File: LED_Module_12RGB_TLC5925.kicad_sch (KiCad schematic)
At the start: 0 parts

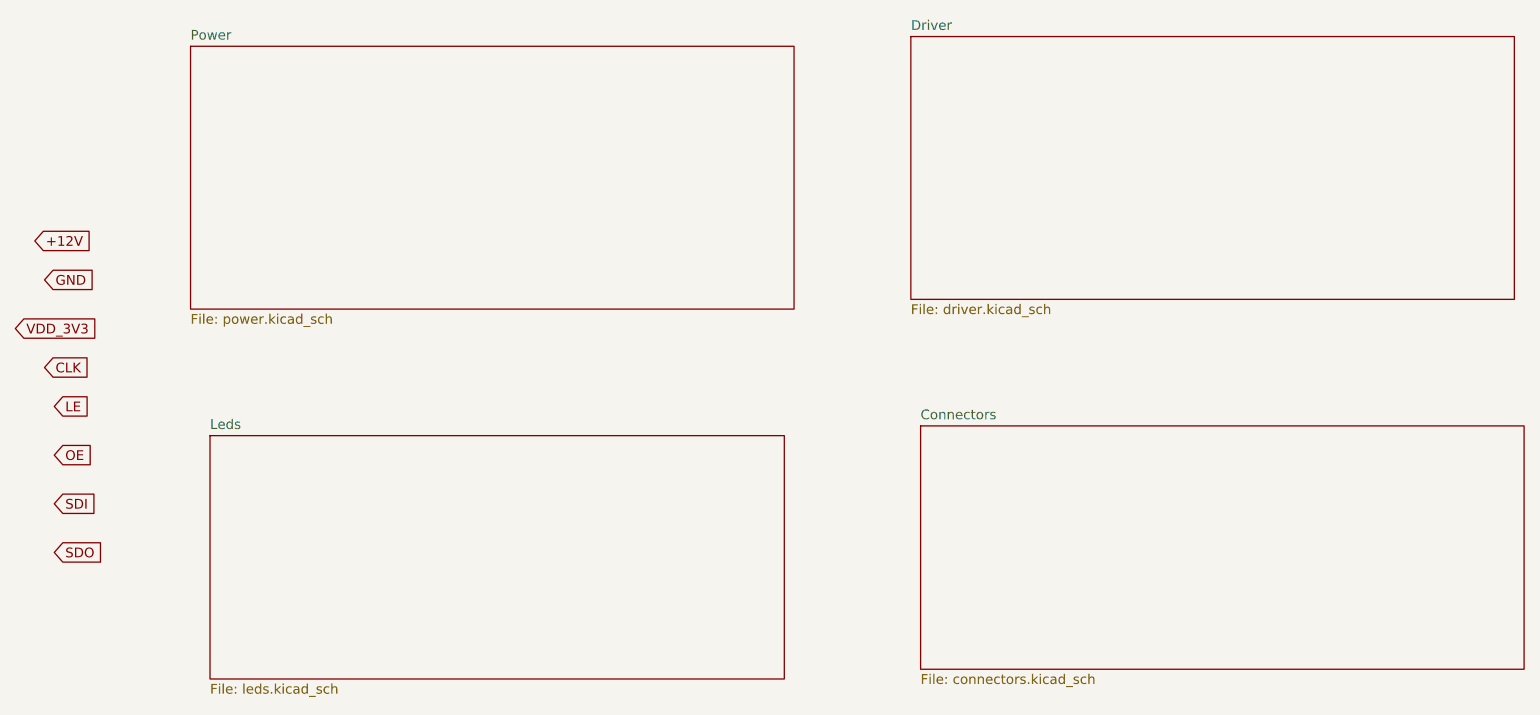
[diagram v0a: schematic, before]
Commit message: v0 2 layer needs grounding islands
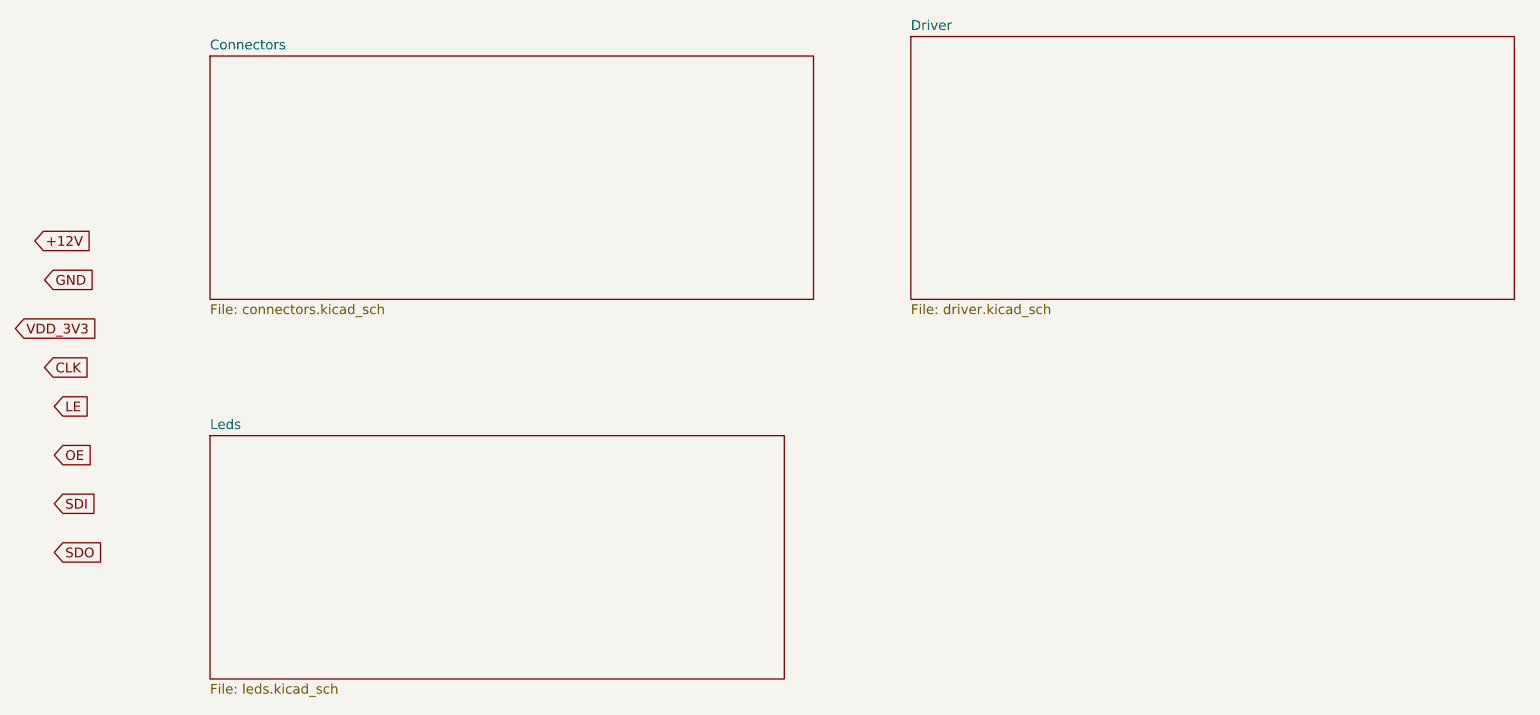
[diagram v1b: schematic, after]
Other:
- removed sheet Power
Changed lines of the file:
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@@
 	)
 	(sheet
-		(at 46.99 26.67)
-		(size 78.74 34.29)
-		(exclude_from_sim no)
-		(in_bom yes)
-		(on_board yes)
-		(dnp no)
-		(fields_autoplaced yes)
-		(stroke
-			(width 0.1524)
-			(type solid)
-		)
-		(fill
-			(color 0 0 0 0)
-		)
-		(property "Sheetname" "Power"
-			(at 46.99 25.9584 0)
-			(show_name no)
-			(do_not_autoplace no)
-			(effects
-				(font
-					(size 1.27 1.27)
-				)
-				(justify left bottom)
-			)
-		)
-		(property "Sheetfile" "power.kicad_sch"
-			(at 46.99 61.5446 0)
-			(show_name no)
-			(do_not_autoplace no)
-			(effects
-				(font
-					(size 1.27 1.27)
-				)
-				(justify left top)
-			)
-		)
-		(instances
-			(project "LED_Module_12RGB_TLC5925"
-				(path "/e21700ea-5a72-4e4b-ac9c-efa1f264ee47"
-					(page "2")
-				)
-			)
-		)
-	)
-	(sheet
-		(at 142.24 76.2)
+		(at 49.53 27.94)
 		(size 78.74 31.75)
 		(exclude_from_sim no)
@@
 		)
 		(property "Sheetname" "Connectors"
-			(at 142.24 75.4884 0)
+			(at 49.53 27.2284 0)
 			(show_name no)
 			(do_not_autoplace no)
@@
 		)
 		(property "Sheetfile" "connectors.kicad_sch"
-			(at 142.24 108.5346 0)
+			(at 49.53 60.2746 0)
 			(show_name no)
 			(do_not_autoplace no)
